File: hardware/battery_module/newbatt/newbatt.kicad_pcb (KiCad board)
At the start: 2 copper layers, 139 x 45 mm, 26 parts, among them J1 Barrel_Jack_MountingPin, J2 Conn_02x10_Odd_Even, U4 BQ24210DQCR

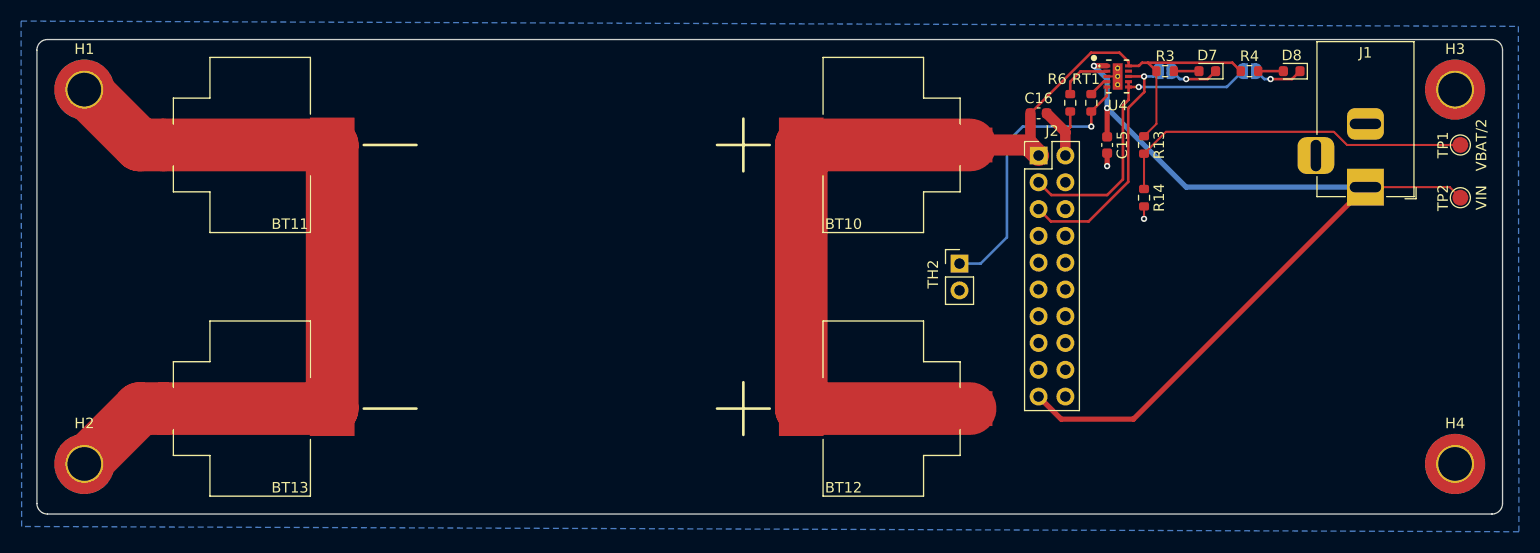
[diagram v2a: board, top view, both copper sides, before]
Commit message: battery switch, fuse, and rerouted traces
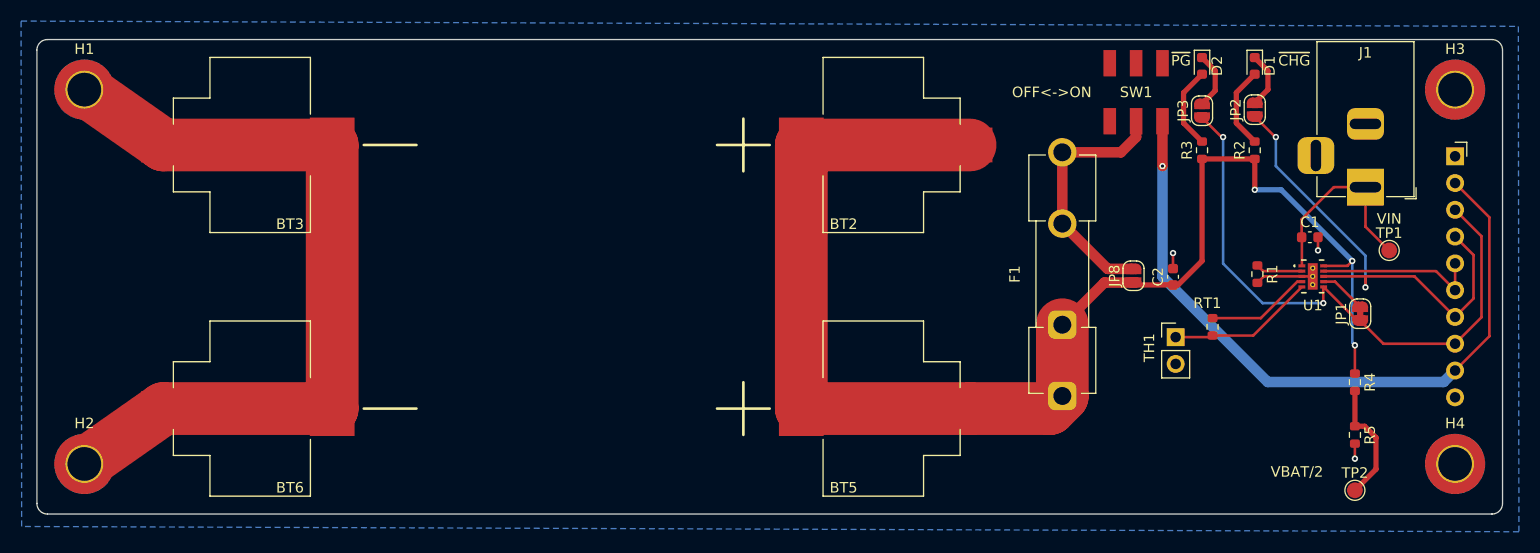
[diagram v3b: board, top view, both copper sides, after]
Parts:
- removed D7, D8: LED, LED_SMD:LED_0603_1608Metric
- removed JP4, JP5: Jumper_2_Small_Open, Jumper:SolderJumper-2_P1.3mm_Open_RoundedPad1.0x1.5mm
- removed R13, R14: 1 MOhm, Resistor_SMD:R_0603_1608Metric
- removed R6: R_Small_US, Resistor_SMD:R_0603_1608Metric
- added D1: LED, LED_SMD:LED_0603_1608Metric, F.Cu at (130.5, 17.5)
- added D2: LED, LED_SMD:LED_0603_1608Metric, F.Cu at (125.5, 17.5)
- added F1: Fuse_Small, Fuse:Fuseholder_Clip-5x20mm_Keystone_3517_Inline_P23.11x6.76mm_D1.70mm_Horizontal, F.Cu at (112.2, 48.8)
- added JP1: SolderJumper_2_Bridged, Jumper:SolderJumper-2_P1.3mm_Bridged_RoundedPad1.0x1.5mm, F.Cu at (140.5, 41.0)
- added JP2: SolderJumper_2_Open, Jumper:SolderJumper-2_P1.3mm_Open_RoundedPad1.0x1.5mm, F.Cu at (130.5, 21.6)
- added JP3: SolderJumper_2_Open, Jumper:SolderJumper-2_P1.3mm_Open_RoundedPad1.0x1.5mm, F.Cu at (125.5, 21.8)
- added JP8: SolderJumper_2_Open, Jumper:SolderJumper-2_P1.3mm_Open_RoundedPad1.0x1.5mm, F.Cu at (119.0, 37.4)
- added R1: R_Small_US, Resistor_SMD:R_0603_1608Metric, F.Cu at (130.8, 37.2)
- added R2: 2 kOhm, Resistor_SMD:R_0603_1608Metric, F.Cu at (130.5, 25.5)
- added R5: 1 MOhm, Resistor_SMD:R_0603_1608Metric, F.Cu at (140.0, 52.5)
- added SW1: SW_Slide_DPDT, JS202011SCQN:JS202011SCQN, F.Cu at (116.8, 22.8)
- J2: value Conn_02x10_Odd_Even -> Conn_01x10; footprint Connector_PinHeader_2.54mm:PinHeader_2x10_P2.54mm_Vertical -> Connector_PinSocket_2.54mm:PinSocket_1x10_P2.54mm_Horizontal
- R4: value 2 kOhm -> 1 MOhm
- TP1: value VBAT sense -> Vin
- TP2: value Vin -> VBAT sense
- moved J2 39.5 mm to (149.5, 26.1)
- moved R4 31.1 mm to (140.0, 47.5), turned to -90 degrees
- moved TP2 29.5 mm to (140.0, 57.8), turned to 0 degrees
- moved U1 26.5 mm to (136.0, 37.5)
- moved RT1 24.2 mm to (126.5, 42.2)
- moved TH1 21.7 mm to (123.0, 43.2)
- moved C1 21.1 mm to (135.7, 33.8), turned to 0 degrees
- moved C2 20.1 mm to (122.8, 37.5), turned to 90 degrees
- moved TP1 12.1 mm to (143.2, 35.0), turned to 0 degrees
- moved R3 8.28 mm to (125.5, 25.5), turned to 90 degrees
- renumbered BT10 to BT2, BT11 to BT3, BT12 to BT5, BT13 to BT6, C15 to C1, C16 to C2, TH2 to TH1, U4 to U1
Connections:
- BT2 pad P1: VOUT -> Net-(JP8-A)
- BT5 pad P1: VOUT -> Net-(JP8-A)
- C2 pad 1: VOUT -> Net-(JP8-A)
- J2 pad 1: VOUT -> 0
- J2 pad 2: 0 -> VOUT
- J2 pad 4: 0 -> /~{CHG}
- J2 pad 5: /~{CHG} -> /VDPM
- J2 pad 6: 0 -> /VDPM
- J2 pad 7: unconnected-(J2-Pin_7-Pad7) -> /~{CHG}
- J2 pad 8: 0 -> /~{PG}
- J2 pad 9: unconnected-(J2-Pin_9-Pad9) -> VOUT
- R3 pad 1: VOUT -> Net-(JP8-A)
- R4 pad 1: VOUT -> Net-(JP8-A)
- R4 pad 2: Net-(D8-A) -> Net-(R4-Pad2)
- TP1 pad 1: Net-(R13-Pad2) -> VIN
- TP2 pad 1: VIN -> Net-(R4-Pad2)
- U1 pad 10: VOUT -> Net-(JP8-A)
- U1 pad 7: /~{PG} -> Net-(JP1-B)
- U1 pad 9: unconnected-(U4-VDPM-Pad9) -> /VDPM
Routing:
- net Net-(JP8-A): track 0.00 -> 132.3 mm, vias 0 -> 3
- net VIN: track 86.5 -> 18.7 mm, vias 2 -> 0
- net Net-(R13-Pad2): track 34.7 -> 0.00 mm
- net VOUT: track 99.6 -> 67.6 mm, vias 0 -> 1
- net /~{PG}: track 30.0 -> 56.8 mm, vias 1 -> 2
- net Net-(JP8-B): track 0.00 -> 24.4 mm
- net /~{CHG}: track 24.2 -> 44.8 mm, vias 1 -> 2
- net /VDPM: track 0.00 -> 15.8 mm
- net Net-(U1-TS): track 27.5 -> 13.9 mm, vias 1 -> 0
- net Net-(R4-Pad2): track 0.00 -> 11.6 mm
- net Net-(U1-VTSB): track 1.96 -> 9.91 mm
- net Net-(D1-A): track 0.00 -> 7.84 mm
- net Net-(D2-A): track 2.39 -> 7.84 mm
- net Net-(D2-K): track 0.00 -> 5.42 mm
- net Net-(D1-K): track 0.00 -> 5.32 mm
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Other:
- board text added: "OFF<->ON"
- board text added: "~{CHG}"
- board text added: "~{PG}"

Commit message: glass fuse and updated footprints
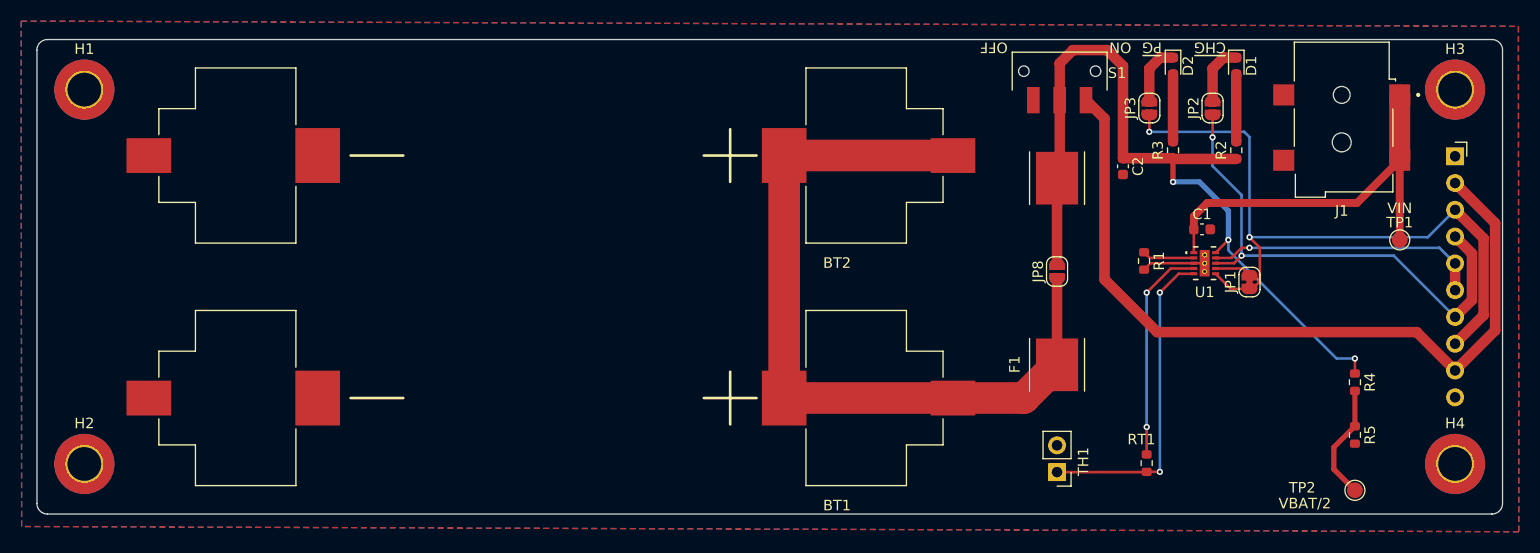
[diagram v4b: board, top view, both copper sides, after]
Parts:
- removed BT3, BT5, BT6: 254TR, Keystone254TR:BAT_254TR
- removed SW1: SW_Slide_DPDT, JS202011SCQN:JS202011SCQN
- added BT1: 3.7 V 2.2 Ah Li-ion 18650, Keystone254TR:BAT_254TR, F.Cu at (83.7, 49.0)
- added S1: JS102011SAQN, JS102011SAQN:SW_JS102011SAQN, F.Cu at (112.0, 18.0)
- BT2: value 254TR -> 3.7 V 2.2 Ah Li-ion 18650
- F1: value Fuse_Small -> 3561KTR; footprint Fuse:Fuseholder_Clip-5x20mm_Keystone_3517_Inline_P23.11x6.76mm_D1.70mm_Horizontal -> 3561KTR:FUSE_3561KTR
- J1: value Barrel_Jack_MountingPin -> 54-00164; footprint Connector_BarrelJack:BarrelJack_Horizontal -> 54-00164:TENSILITY_54-00164
- R1: value R_Small_US -> 500 Ohm
- moved TH1 17.0 mm to (111.8, 56.0), turned to 180 degrees
- moved RT1 14.4 mm to (120.2, 55.2)
- moved BT2 11.9 mm to (83.7, 26.0), turned to 180 degrees
- moved C2 11.5 mm to (118.0, 27.0), turned to -90 degrees
- moved JP1 10.9 mm to (130.0, 38.0)
- moved R1 10.8 mm to (120.0, 36.0)
- moved U1 10.3 mm to (125.8, 36.2)
- moved C1 10.3 mm to (125.5, 33.0)
- moved JP8 7.26 mm to (111.8, 37.0)
- moved J1 6.88 mm to (138.8, 22.5), turned to 180 degrees
- moved JP3 5.01 mm to (120.5, 21.5)
- moved JP2 4.00 mm to (126.5, 21.5)
- moved F1 3.00 mm to (111.8, 45.9)
- moved D2 2.75 mm to (122.8, 17.5)
- moved R3 2.75 mm to (122.8, 25.5)
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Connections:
- C2 pad 1: Net-(JP8-A) -> Net-(JP8-B)
- F1 pad 1: Net-(JP8-A) -> Net-(BT1-+)
- JP8 pad 1: Net-(JP8-A) -> Net-(BT1-+)
- R2 pad 1: Net-(JP8-A) -> Net-(JP8-B)
- R3 pad 1: Net-(JP8-A) -> Net-(JP8-B)
- R4 pad 1: Net-(JP8-A) -> Net-(JP8-B)
- U1 pad 10: Net-(JP8-A) -> Net-(JP8-B)
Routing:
- net Net-(JP8-A): track 132.3 -> 0.00 mm, vias 3 -> 0
- net 0: track 85.0 -> 6.00 mm, vias 3 -> 0
- net Net-(BT1-+): track 0.00 -> 74.4 mm
- net Net-(JP8-B): track 24.4 -> 77.2 mm, vias 0 -> 3
- net VIN: track 18.7 -> 38.9 mm
- net Net-(U1-TS): track 13.9 -> 30.7 mm, vias 0 -> 2
- net Net-(U1-VTSB): track 9.91 -> 20.8 mm, vias 0 -> 2
- net /VDPM: track 15.8 -> 26.3 mm, vias 0 -> 1
- net /~{PG}: track 56.8 -> 66.0 mm
- net VOUT: track 67.6 -> 75.6 mm, vias 1 -> 0
- net /~{CHG}: track 44.8 -> 48.9 mm
- net Net-(D2-A): track 7.84 -> 6.39 mm
- net Net-(D1-A): track 7.84 -> 6.39 mm
- net Net-(JP1-B): track 4.46 -> 3.49 mm
- net Net-(R4-Pad2): track 11.6 -> 11.1 mm
- added copper zone on F.Cu, net 0
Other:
- board text added: "OFF"
- board text added: "ON"
- board text removed: "OFF<->ON"

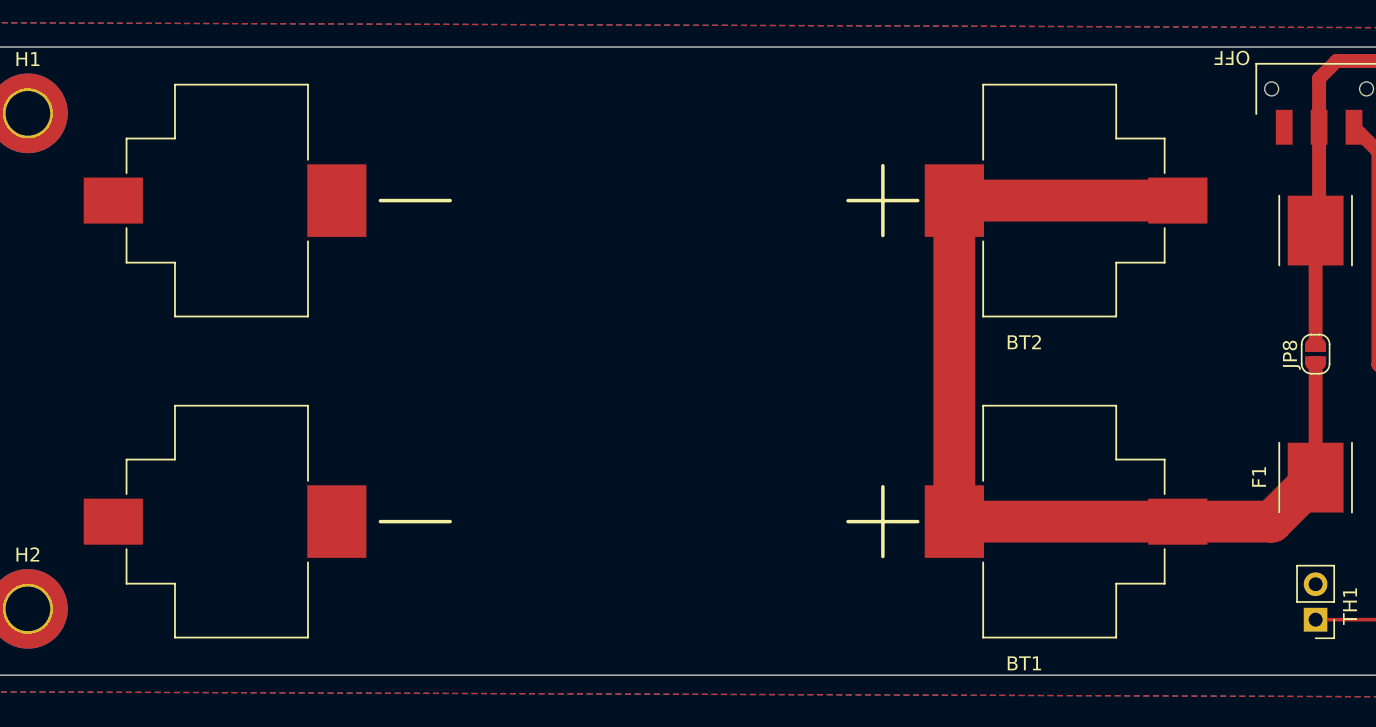
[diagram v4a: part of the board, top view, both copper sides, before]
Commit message: Updated BoM with LCSC, Digikey. Updated 18650 battery clip footprint with 67.2mm spacing for 65mm and 67mm cells
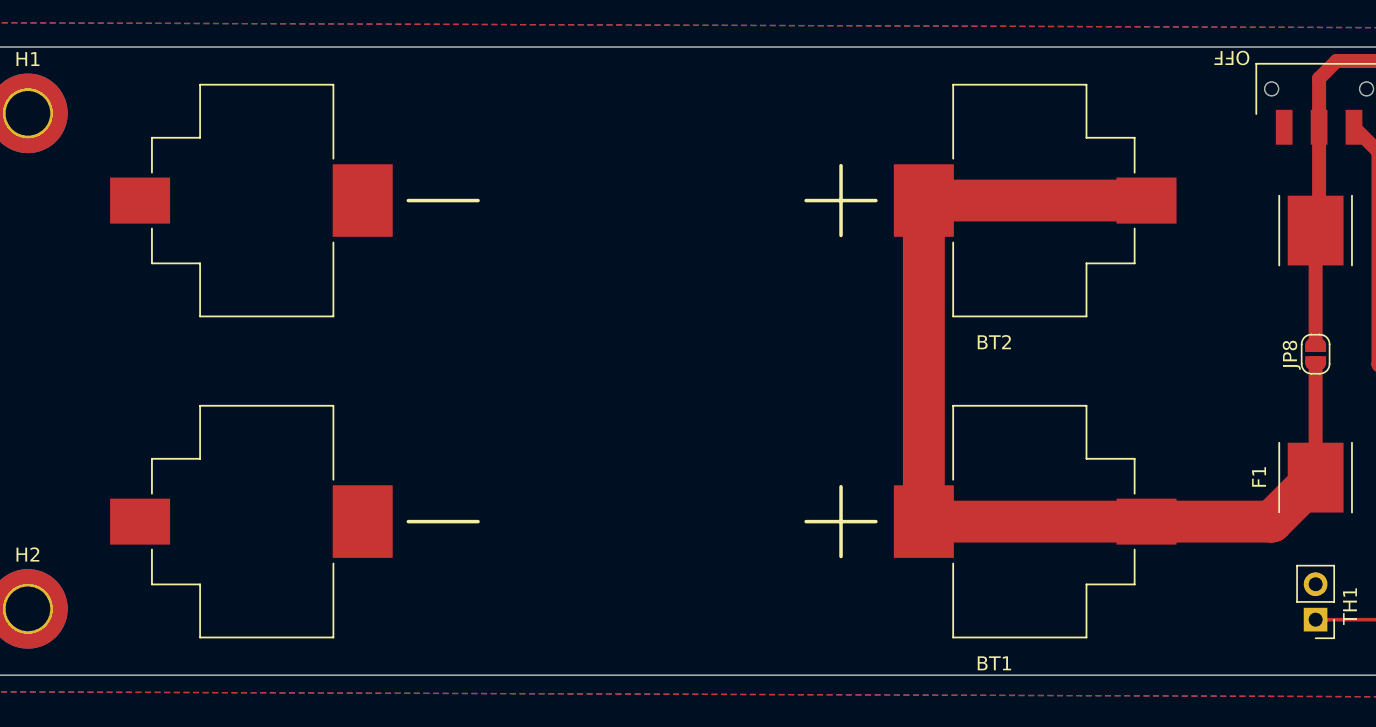
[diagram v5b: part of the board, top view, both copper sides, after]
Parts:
- BT1, BT2: footprint Keystone254TR:BAT_254TR -> Keystone254TR:BAT_254TR_67mm
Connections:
- net VIN renamed Net-(U1-VBUS)
- net VOUT renamed Net-(J2-Pin_2)
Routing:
- net Net-(BT1-+): track 74.4 -> 76.5 mm

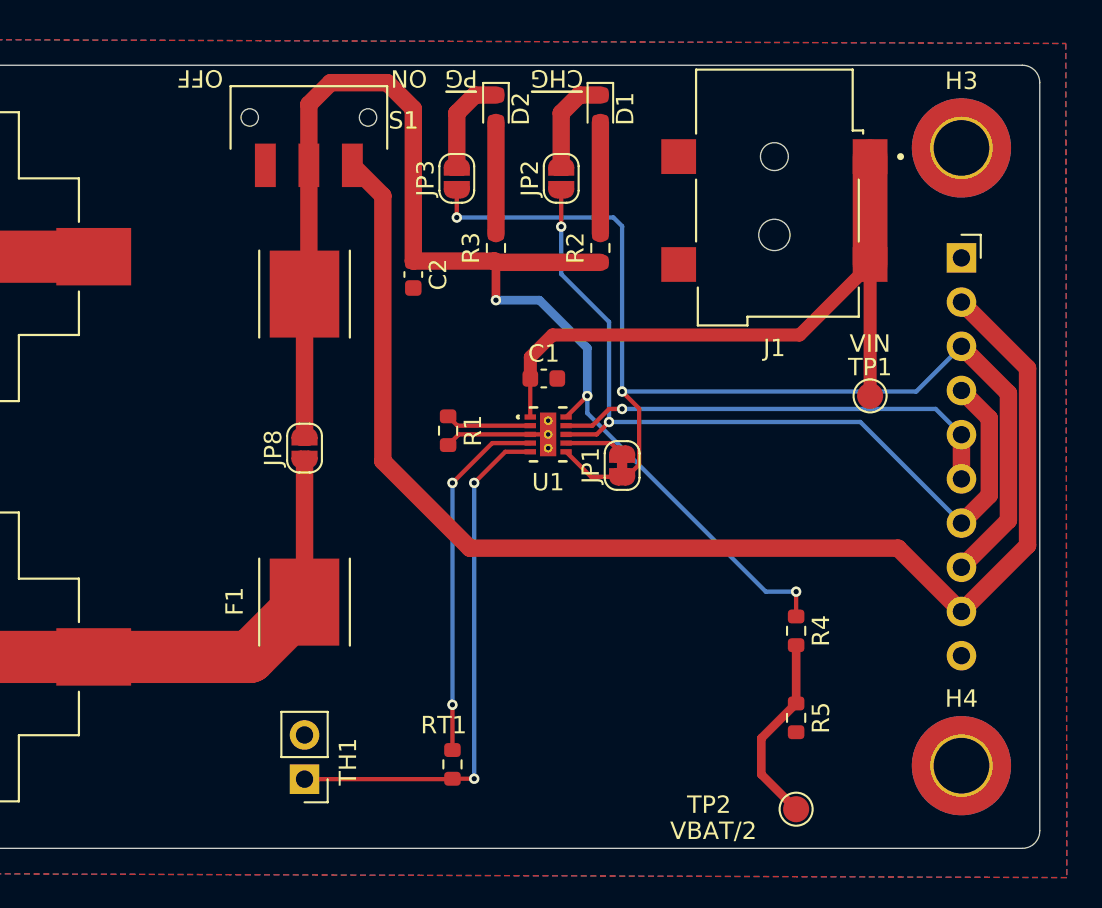
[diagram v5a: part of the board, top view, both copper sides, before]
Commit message: Reviewed with John, updated VDPM and resistor values and barrel jack
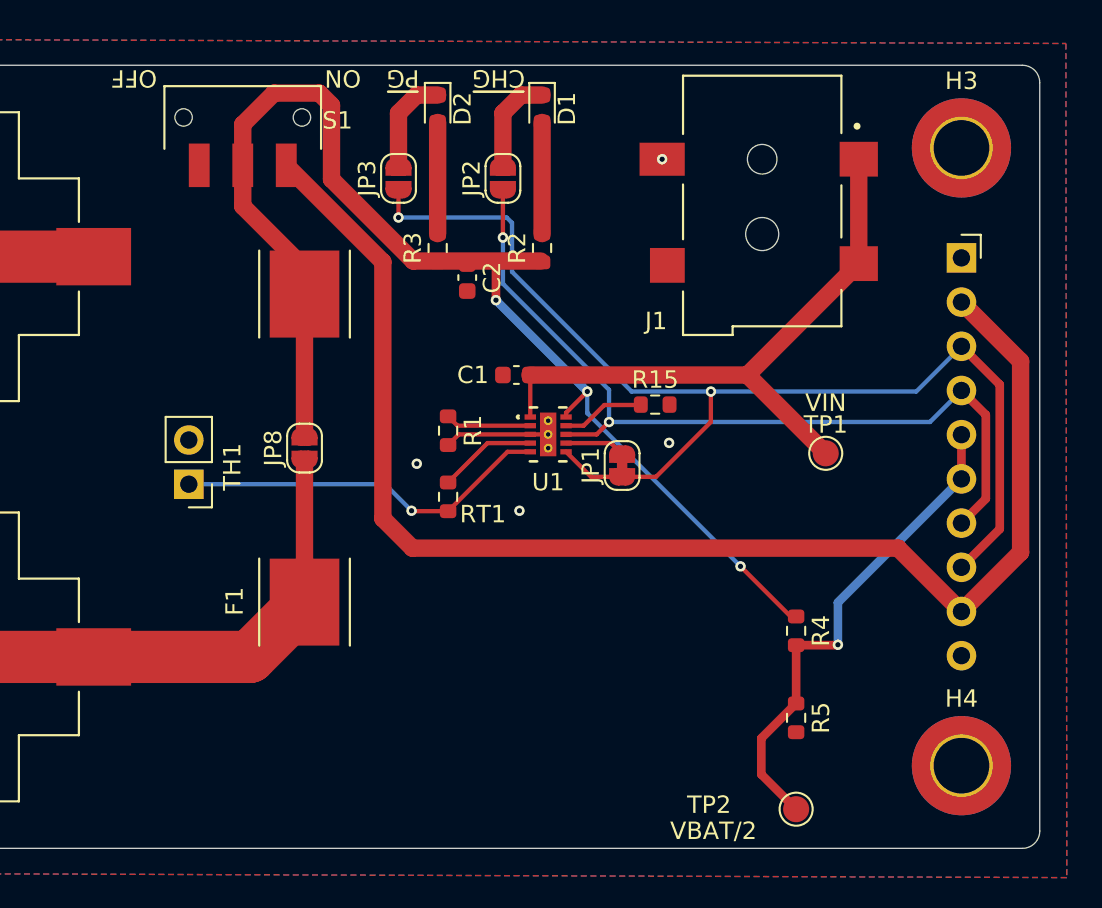
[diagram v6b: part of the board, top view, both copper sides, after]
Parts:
- added R15: 500 Ohm, Resistor_SMD:R_0603_1608Metric, F.Cu at (131.9, 34.5)
- J1: value 54-00164 -> DC050-T; footprint 54-00164:TENSILITY_54-00164 -> DC050-T:DC050-T
- R1: value 500 Ohm -> 680 Ohm
- moved TH1 18.2 mm to (105.1, 39.1)
- moved RT1 15.4 mm to (120.0, 39.8)
- moved J1 9.57 mm to (133.5, 30.5), turned to 90 degrees
- moved TP1 4.17 mm to (141.7, 37.3)
- moved S1 3.80 mm to (108.2, 18.0)
- moved D1 3.35 mm to (125.4, 17.5)
- moved D2 3.35 mm to (119.4, 17.5)
- moved JP2 3.35 mm to (123.2, 21.5)
- moved JP3 3.35 mm to (117.2, 21.5)
- moved R2 3.35 mm to (125.4, 25.5)
- moved R3 3.35 mm to (119.4, 25.5)
- moved C2 3.10 mm to (121.1, 27.2)
- moved C1 1.59 mm to (123.9, 32.8), turned to 180 degrees
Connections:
- J2 pad 5: /VDPM -> /VBAT/2
- J2 pad 6: /VDPM -> /VBAT/2
- R4 pad 2: Net-(R4-Pad2) -> /VBAT/2
- R5 pad 1: Net-(R4-Pad2) -> /VBAT/2
- TP2 pad 1: Net-(R4-Pad2) -> /VBAT/2
- U1 pad 9: /VDPM -> Net-(U1-VDPM)
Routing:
- net /VBAT/2: track 0.00 -> 28.5 mm, vias 0 -> 1
- net /VDPM: track 26.3 -> 0.00 mm, vias 1 -> 0
- net Net-(U1-VTSB): track 20.8 -> 5.66 mm, vias 2 -> 0
- net Net-(R4-Pad2): track 11.1 -> 0.00 mm
- net Net-(U1-TS): track 30.7 -> 21.7 mm, vias 2 -> 1
- net Net-(U1-VDPM): track 0.00 -> 4.71 mm
- net Net-(JP8-B): track 77.2 -> 73.3 mm
- net Net-(J2-Pin_2): track 75.6 -> 78.8 mm
- net Net-(U1-VBUS): track 38.9 -> 36.3 mm
- net /~{PG}: track 66.0 -> 67.3 mm
- net 0: vias 0 -> 4
